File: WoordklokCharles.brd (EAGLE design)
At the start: 102 x 40 mm, 33 parts, among them IC1 74HC595N, IC2 74HC595N, IC3 78L33, IC4 MCP1702-5002, Q1 16MHz, U1 ATMEGA328P, X2 22-23-2021

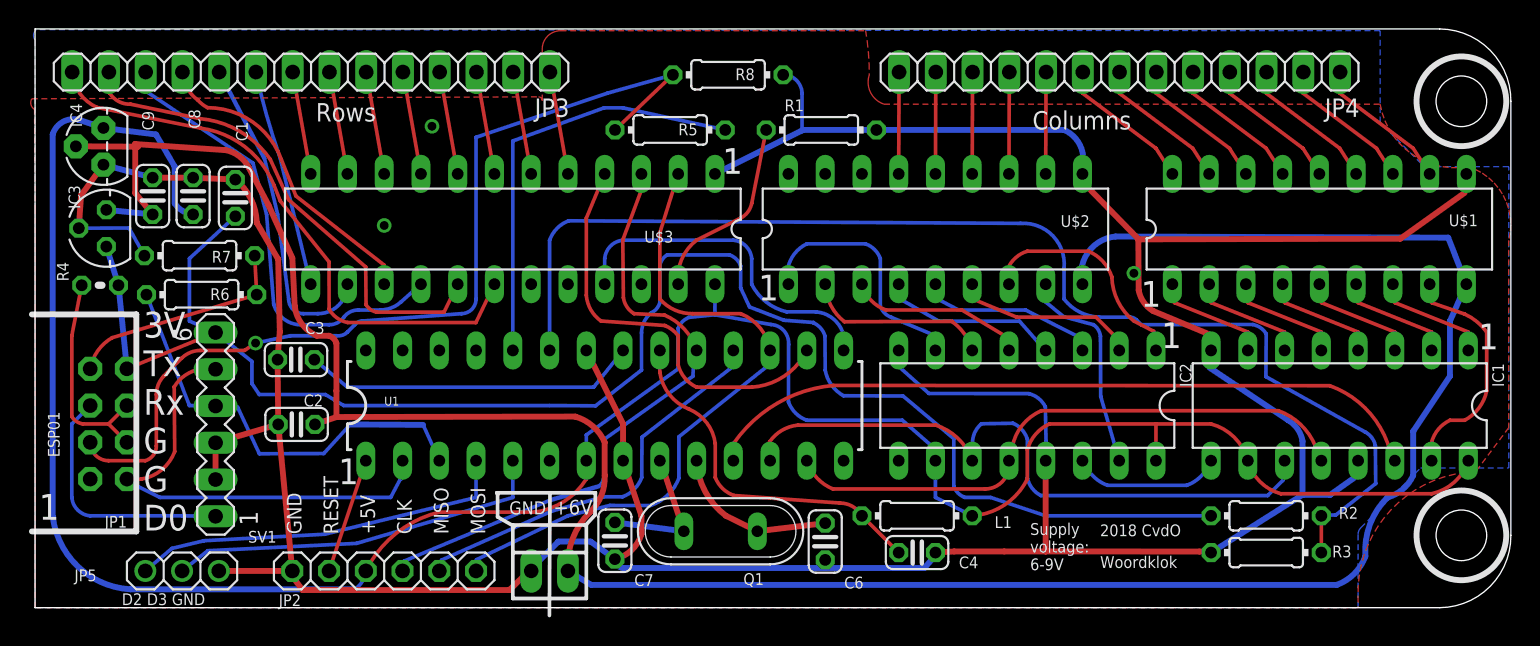
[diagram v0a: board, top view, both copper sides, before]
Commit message: V3.0 of CADsoft Eagle files,
V3.0: changed IC3 to MCP1702-33
V2.0: added pull-up resistors for ESP01, several minor corrections
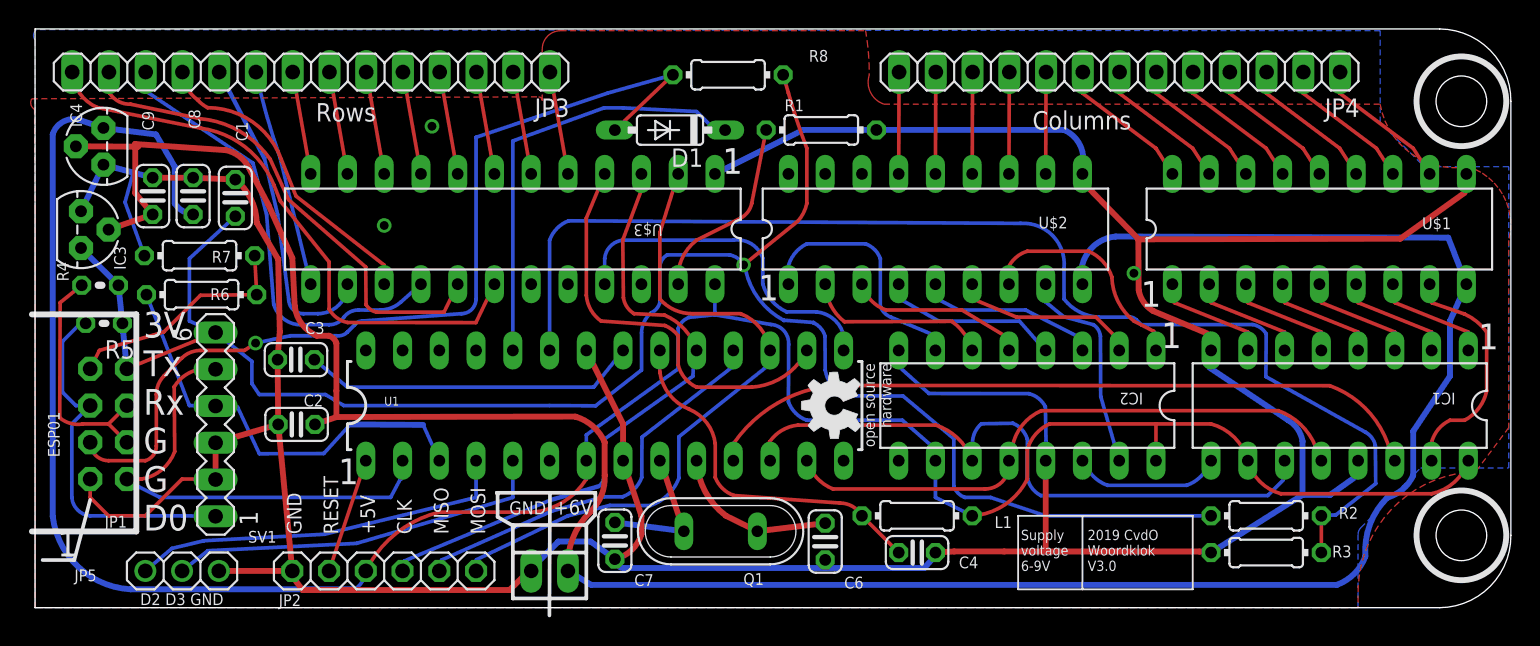
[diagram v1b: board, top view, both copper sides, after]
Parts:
- added D1: 1N4148DO35-7, diode:DO35-7
- added U$4: (no value), oshw:OSHW_5MM
- IC3: value 78L33 -> MCP1702-3302; device v-reg:78LXX -> adafruit:TO92
- R2: value (none) -> 120k
- R5: value 1k7 -> 10k; device rcl:0204/7 -> rcl:0204V
- R8: value 3k3 -> 10k
- U1: value ATMEGA328P -> ATMEGA88
- moved R5 41.3 mm to (4.77, 19.7)
- moved IC3 1.75 mm to (3.17, 26.1), turned to 270 degrees
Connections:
- net +3V3: now also IC3.3, R5.1, R8.2; no longer IC3.OUT
- net +6V: now also IC3.2; no longer IC3.IN
- net GND: now also IC3.1; no longer IC3.GND, R8.2
- net GPIO2: now also D1.A; no longer R5.2
- net N$29: now also R5.2
- net N$65: now also D1.C; no longer R5.1
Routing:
- net +3V3: track 116.5 -> 132.7 mm, vias 0 -> 1
- net N$29: track 17.3 -> 25.3 mm
- net GND: track 266.3 -> 272.5 mm
- net N$30: track 15.4 -> 16.9 mm
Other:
- board text added: "2019 CvdO Woordklok V3.0"
- board text added: "Supply voltage 6-9V"
- board text removed: "2018 CvdO"
- board text removed: "Supply voltage: 6-9V"
- board text removed: "Woordklok"
